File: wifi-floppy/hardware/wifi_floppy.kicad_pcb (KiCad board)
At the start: 2 copper layers, 96 x 62 mm, 13 parts, among them J1 FLOPPY34, J2 PWR-BERG, Q1 BSS138, Q2 BSS138, Q3 BSS138, Q4 BSS138, Q5 BSS138, Q6 BSS138, U1 Pico2W/PicoPlus2W, U2 74LVC541A

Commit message: [REV B] New PCB version.
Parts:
- added BZ1: Buzzer, wifi-floppy-lib:Buzzer_TDK_PS1240P02BT_D12.2mm_H6.5mm, F.Cu at (116.1, 117.6)
- added D2: LED, wifi-floppy-lib:LED_1206_3216Metric_Pad1.42x1.75mm_HandSolder, F.Cu at (124.0, 107.7)
- added J3: Conn_01x04, wifi-floppy-lib:PinHeader_1x04_P2.54mm_Vertical, F.Cu at (126.5, 103.2)
- added J4: Conn_01x04, wifi-floppy-lib:PinHeader_1x04_P2.54mm_Vertical, F.Cu at (114.0, 103.2)
- added Q7: BSS138, wifi-floppy-lib:SOT-23, F.Cu at (127.4, 113.3)
- added Q8: BSS138, wifi-floppy-lib:SOT-23, F.Cu at (127.4, 116.7)
- added R1: 1k, wifi-floppy-lib:R_1206_3216Metric_Pad1.30x1.75mm_HandSolder, F.Cu at (115.5, 132.8)
- added R2: 1k, wifi-floppy-lib:R_1206_3216Metric_Pad1.30x1.75mm_HandSolder, F.Cu at (115.5, 129.6)
- added R3: 1k, wifi-floppy-lib:R_1206_3216Metric_Pad1.30x1.75mm_HandSolder, F.Cu at (115.5, 126.0)
- added R4: 1k, wifi-floppy-lib:R_1206_3216Metric_Pad1.30x1.75mm_HandSolder, F.Cu at (128.4, 107.6)
- added R5: 1k, wifi-floppy-lib:R_1206_3216Metric_Pad1.30x1.75mm_HandSolder, F.Cu at (136.4, 110.0)
- added R6: 10k, wifi-floppy-lib:R_1206_3216Metric_Pad1.30x1.75mm_HandSolder, F.Cu at (134.2, 110.0)
- C1: value 100n -> 100nF; footprint Capacitor_SMD:C_0603 -> wifi-floppy-lib:C_1206_3216Metric_Pad1.33x1.80mm_HandSolder
- C3: value 10u -> 10uF; footprint Capacitor_SMD:C_0805 -> wifi-floppy-lib:C_1206_3216Metric_Pad1.33x1.80mm_HandSolder
- D1: footprint Diode_SMD:D_SMA -> wifi-floppy-lib:D_SMA_Handsoldering
- J1: value FLOPPY34 -> Conn_02x17_Odd_Even; footprint Connector_PinHeader_2.54mm:PinHeader_2x17 -> wifi-floppy-lib:IDC-Header_2x17_P2.54mm_Vertical
- J2: value PWR-BERG -> Conn_01x04; footprint Connector_PinHeader_2.54mm:PinHeader_1x04 -> wifi-floppy-lib:PinHeader_1x04_P2.54mm_Horizontal
- Q1, Q2, Q3, Q4, Q5, Q6: footprint Package_TO_SOT_SMD:SOT-23 -> wifi-floppy-lib:SOT-23
- U1: value Pico2W/PicoPlus2W -> RaspberryPi_Pico_W; footprint wifi_floppy:Pico2W_THT -> wifi-floppy-lib:RaspberryPi_Pico_W_SMD_HandSolder
- U2: footprint Package_SO:SOIC-20W -> wifi-floppy-lib:SOIC-20W_7.5x15.4mm_P1.27mm
- moved D1 55.9 mm to (134.2, 146.8), turned to -90 degrees
- moved U1 26.5 mm to (149.7, 128.0)
- moved J2 21.9 mm to (129.2, 142.4), turned to -90 degrees
- moved C1 21.3 mm to (130.6, 120.0), turned to 180 degrees
- moved U2 20.3 mm to (127.6, 130.0)
- moved C3 13.2 mm to (128.0, 139.2), turned to 180 degrees
- moved Q2 7.97 mm to (118.6, 108.2), turned to 180 degrees
- moved Q1 2.35 mm to (114.7, 108.2), turned to 180 degrees
- moved Q6 2.32 mm to (114.8, 146.8), turned to 180 degrees
- moved Q3 2.19 mm to (114.8, 136.4), turned to 180 degrees
- moved Q5 2.16 mm to (114.8, 143.3), turned to 180 degrees
- moved Q4 2.15 mm to (114.8, 139.9), turned to 180 degrees
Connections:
- net +3V3 renamed +3.3V
- net VSYS renamed /VSYS
- J1 pad 14: (no net) -> unconnected-(J1-Pin_14-Pad14)
- J1 pad 4: (no net) -> unconnected-(J1-Pin_4-Pad4)
- J1 pad 6: (no net) -> unconnected-(J1-Pin_6-Pad6)
- J2 pad 4: +12V -> unconnected-(J2-Pin_4-Pad4)
- U1 pad 19: (no net) -> unconnected-(U1-GPIO14-Pad19)
- U1 pad 20: (no net) -> unconnected-(U1-GPIO15-Pad20)
- U1 pad 21: (no net) -> unconnected-(U1-GPIO16-Pad21)
- U1 pad 22: (no net) -> unconnected-(U1-GPIO17-Pad22)
- U1 pad 24: (no net) -> OLED_SDA
- U1 pad 25: (no net) -> OLED_SCL
- U1 pad 26: (no net) -> unconnected-(U1-GPIO20-Pad26)
- U1 pad 27: (no net) -> BUZZER
- U1 pad 29: (no net) -> ACT_LED
- U1 pad 30: (no net) -> unconnected-(U1-RUN-Pad30)
- U1 pad 31: (no net) -> unconnected-(U1-GPIO26_ADC0-Pad31)
- U1 pad 32: (no net) -> unconnected-(U1-GPIO27_ADC1-Pad32)
- U1 pad 34: (no net) -> unconnected-(U1-GPIO28_ADC2-Pad34)
- U1 pad 35: (no net) -> unconnected-(U1-ADC_VREF-Pad35)
- U1 pad 37: (no net) -> unconnected-(U1-3V3_EN-Pad37)
- U1 pad 40: (no net) -> unconnected-(U1-VBUS-Pad40)
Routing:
- net OLED_SDA: track 0.00 -> 76.1 mm
- net OLED_SCL: track 0.00 -> 70.1 mm
- net ACT_LED: track 0.00 -> 56.8 mm
- net GND: track 14.6 -> 61.4 mm
- net INDEX: track 68.6 -> 23.5 mm, vias 2 -> 0
- net BUZZER: track 0.00 -> 44.1 mm, vias 0 -> 1
- net SIDE: track 40.4 -> 9.51 mm
- net WGATE: track 39.1 -> 10.0 mm
- net CHNG: track 55.2 -> 27.6 mm
- net WPROT: track 52.7 -> 26.0 mm, vias 2 -> 0
- net WDATA: track 37.8 -> 11.8 mm
- net SIDE_B: track 51.2 -> 25.7 mm
- net RDATA: track 53.0 -> 28.0 mm, vias 2 -> 0
- net TRK0: track 62.6 -> 38.2 mm, vias 4 -> 0
- net WDATA_B: track 41.1 -> 16.8 mm
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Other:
- board size 96 x 62 mm -> 61.4 x 54 mm
- board text added: "+5V"
- board text added: "1"
- board text added: "3V3"
- board text added: "GND"
- board text added: "K"
- board text added: "SCL"
- board text added: "SDA"

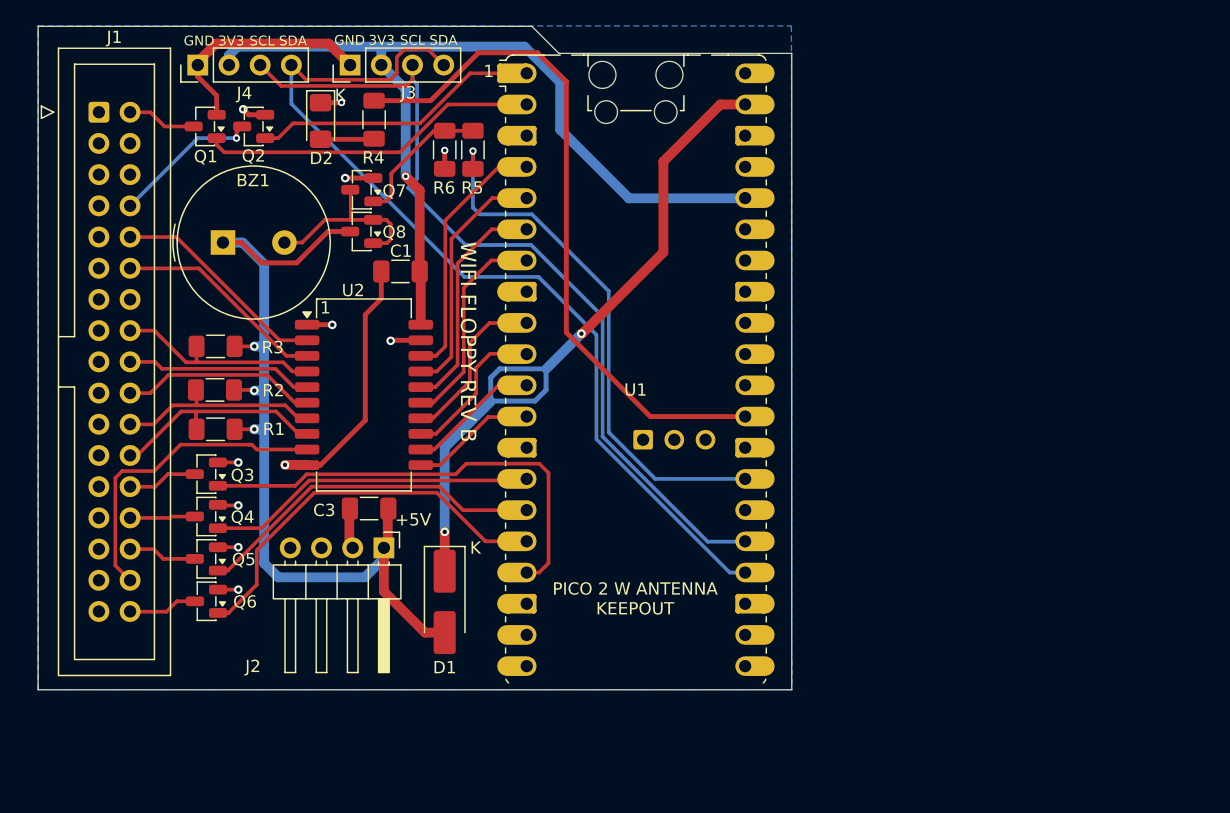
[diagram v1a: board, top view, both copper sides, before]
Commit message: Add some pullup resistors to other inputs
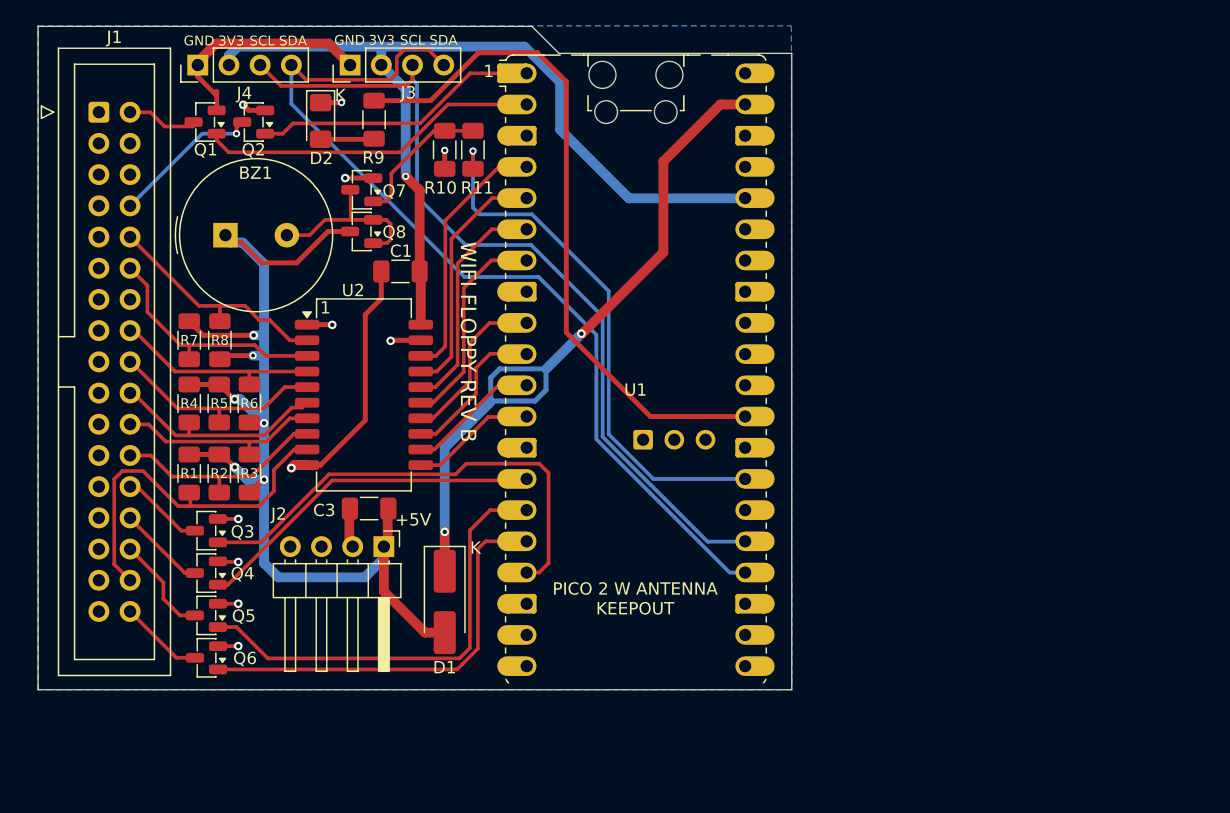
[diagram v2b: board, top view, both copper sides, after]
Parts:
- added R1: 1k, wifi-floppy-lib:R_1206_3216Metric_Pad1.30x1.75mm_HandSolder, F.Cu at (113.3, 136.4)
- added R4: 1k, wifi-floppy-lib:R_1206_3216Metric_Pad1.30x1.75mm_HandSolder, F.Cu at (113.3, 130.7)
- added R5: 1k, wifi-floppy-lib:R_1206_3216Metric_Pad1.30x1.75mm_HandSolder, F.Cu at (115.8, 130.7)
- added R7: 1k, wifi-floppy-lib:R_1206_3216Metric_Pad1.30x1.75mm_HandSolder, F.Cu at (113.3, 125.5)
- added R8: 1k, wifi-floppy-lib:R_1206_3216Metric_Pad1.30x1.75mm_HandSolder, F.Cu at (115.8, 125.5)
- moved R3 7.35 mm to (118.2, 136.4), turned to 90 degrees
- moved R6 5.40 mm to (118.2, 130.7), turned to 90 degrees
- moved Q3 4.60 mm to (114.8, 141.1)
- moved Q4 4.60 mm to (114.8, 144.5)
- moved Q5 4.60 mm to (114.8, 147.9)
- moved Q6 4.60 mm to (114.8, 151.4)
- moved R2 3.61 mm to (115.8, 136.4), turned to -90 degrees
- moved BZ1 0.63 mm to (116.3, 117.0)
- moved Q1 0.36 mm to (114.7, 107.8)
- moved Q2 0.36 mm to (118.6, 107.8)
- moved J2 0.10 mm to (129.2, 142.3)
- renumbered R6 to R10, R5 to R11, R1 to R2, R2 to R3, R3 to R6, R4 to R9
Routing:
- net +5V: track 74.3 -> 93.5 mm, vias 3 -> 6
- net RDATA: track 28.0 -> 36.0 mm
- net SIDE_B: track 25.7 -> 30.0 mm
- net RDATA_B: track 5.60 -> 8.29 mm
- net DIR_B: track 15.3 -> 17.9 mm
- net SEL1_B: track 17.4 -> 19.8 mm
- net STEP_B: track 16.0 -> 18.0 mm
- net TRK0: track 38.2 -> 40.1 mm
- net WPROT: track 26.0 -> 27.9 mm
- net WPROT_B: track 5.32 -> 7.15 mm
- net RDY: track 31.7 -> 33.4 mm
- net SEL0_B: track 17.9 -> 19.1 mm
- net RDY_B: track 5.64 -> 6.85 mm
- net TRK0_B: track 5.74 -> 6.76 mm
- net OLED_SCL: track 70.1 -> 69.5 mm
